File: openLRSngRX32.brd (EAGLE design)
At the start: 40.3 x 36.8 mm, 19 parts, among them IC1 STM32F10XCXT6, IC2 REG1117

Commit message: - remove project - working onwards...
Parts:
- added C1, C10, C11, C2, C3, C4, C5, C6, C7, C8, C9: (no value), SparkFun-Capacitors:0805
- added JP4: (no value), SparkFun-Connectors:1X04
- added JP5, JP6: (no value), SparkFun-Connectors:1X06
- added JP7, JP8: (no value), SparkFun-Connectors:1X02
- added R13, R14, R15, R16: (no value), SparkFun-Resistors:0805
- added U1: MPU-6000QFN-24, SparkFun-Sensors:QFN-24-TESTING
- added Y1: (no value), crystal_3225:CRYSTAL-SMD-5X3
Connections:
- new net BOOT0: IC1.44, JP7.2, R15.2
- new net DTR: JP5.6
- new net MPUINT: U1.12
- new net N$14: C1.2, U1.10
- new net N$15: C2.2, U1.20
- new net N$16: C4.1, IC1.5, Y1.3
- new net N$17: C3.1, IC1.6, Y1.1
- new net N$29: JP5.2
- new net N$35: JP6.3
- new net PPM: IC1.29, JP6.6
- new net RESET: C11.1, IC1.7, JP8.1, R16.1
- new net RX: IC1.31, JP5.4
- new net SCL: IC1.21, JP4.3, R13.1, U1.23
- new net SDA: IC1.22, JP4.2, R14.1, U1.24
- new net TX: IC1.30, JP5.5
- net 3V3: now also C10.1, C5.1, C6.1, C7.1, C8.1, C9.1, JP4.4, JP5.3, JP7.1, R13.2, R14.2, R16.2, U1.13, U1.8
- net GND: now also C1.1, C10.2, C11.2, C2.1, C3.2, C4.2, C5.2, C6.2, C7.2, C8.2, C9.2, JP4.1, JP5.1, JP6.1, JP6.4, JP8.2, R15.1, U1.1, U1.11, U1.18, U1.9, Y1.2, Y1.4
- net VCC: now also JP6.2, JP6.5
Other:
- board size 40.3 x 36.8 mm -> 48.6 x 48.2 mm

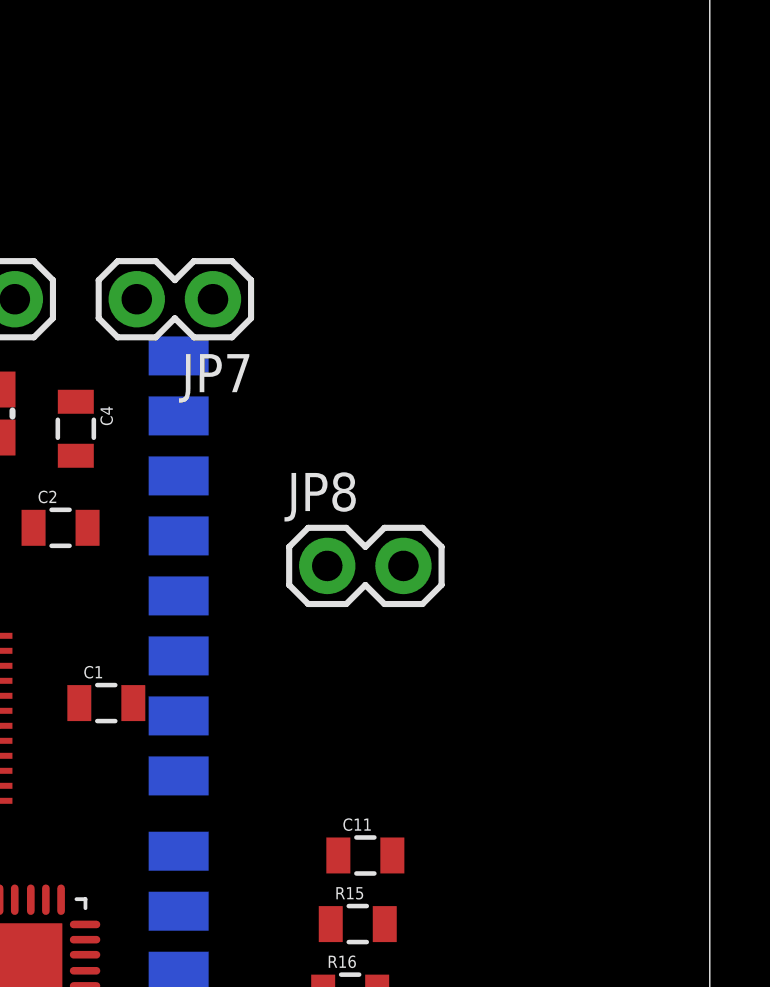
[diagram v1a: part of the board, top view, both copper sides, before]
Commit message: some more caps
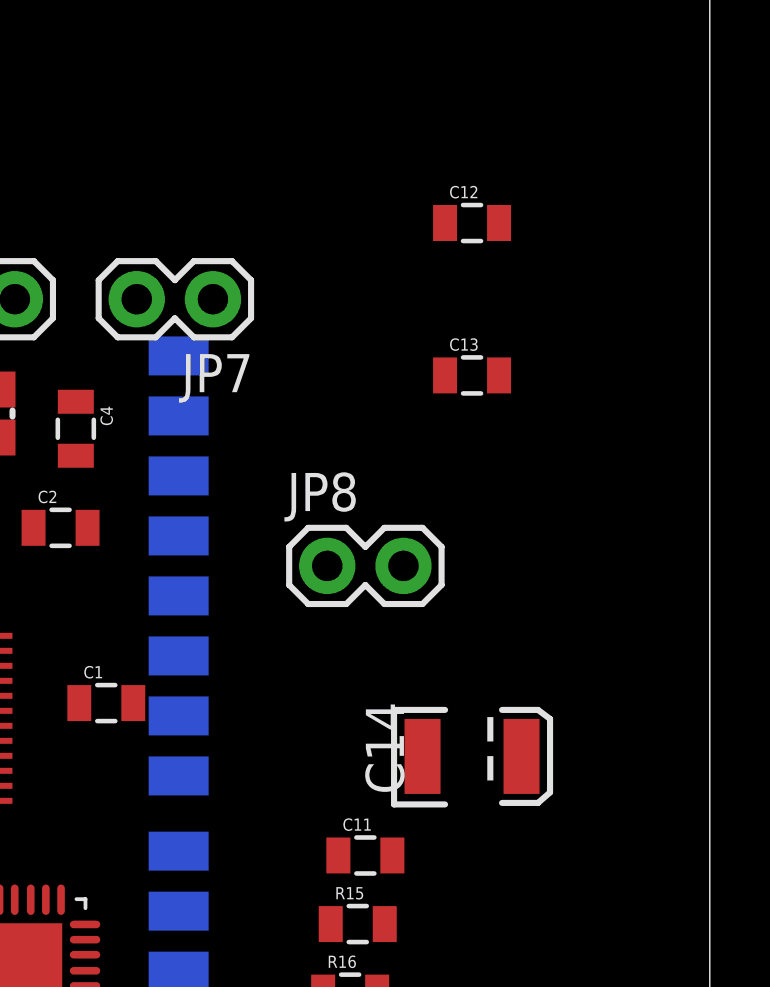
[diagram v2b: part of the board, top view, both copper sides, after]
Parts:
- added C12, C13: (no value), SparkFun-Capacitors:0805
- added C14: 47uF, SparkFun-Capacitors:EIA3528
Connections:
- net 3V3: now also C14.A
- net GND: now also C12.2, C13.2, C14.C
- net VCC: now also C12.1, C13.1
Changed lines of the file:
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@@
 <element name="JP7" library="SparkFun-Connectors" package="1X02" value="" x="32.004" y="35.56" rot="R180"/>
 <element name="JP8" library="SparkFun-Connectors" package="1X02" value="" x="35.814" y="26.67"/>
+<element name="C12" library="SparkFun-Capacitors" package="0805" value="" x="40.64" y="38.1"/>
+<element name="C13" library="SparkFun-Capacitors" package="0805" value="" x="40.64" y="33.02"/>
+<element name="C14" library="SparkFun-Capacitors" package="EIA3528" value="47uF" x="40.64" y="20.32">
+<attribute name="PROD_ID" value="CAP-08310" x="40.64" y="20.32" size="1.778" layer="27" display="off"/>
+</element>
 </elements>
 <signals>
@@
 <contactref element="C11" pad="2"/>
 <contactref element="JP8" pad="2"/>
+<contactref element="C13" pad="2"/>
+<contactref element="C12" pad="2"/>
+<contactref element="C14" pad="C"/>
+<wire x1="30.86" y1="31.67" x2="38.354" y2="26.67" width="0" layer="19" extent="16-16"/>
 <wire x1="27.432" y1="30.342" x2="30.86" y2="31.67" width="0" layer="19" extent="1-16"/>
 <wire x1="26.024" y1="27.94" x2="27.432" y2="30.342" width="0" layer="19" extent="1-1"/>
@@
 <wire x1="2.54" y1="5.08" x2="2.54" y2="7.62" width="0" layer="19" extent="1-1"/>
 <wire x1="2.54" y1="2.54" x2="2.54" y2="5.08" width="0" layer="19" extent="1-1"/>
-<wire x1="38.354" y1="26.67" x2="2.54" y2="2.54" width="0" layer="19" extent="1-1"/>
+<wire x1="41.54" y1="38.1" x2="2.54" y2="2.54" width="0" layer="19" extent="1-1"/>
+<wire x1="41.54" y1="33.02" x2="41.54" y2="38.1" width="0" layer="19" extent="1-1"/>
+<wire x1="38.99" y1="20.32" x2="41.54" y2="33.02" width="0" layer="19" extent="1-1"/>
 </signal>
 <signal name="VCC">
@@
 <contactref element="JP6" pad="5"/>
 <contactref element="JP6" pad="2"/>
+<contactref element="C12" pad="1"/>
+<contactref element="C13" pad="1"/>
+<wire x1="5.08" y1="33.02" x2="12.7" y2="33.02" width="0" layer="19" extent="1-1"/>
+<wire x1="5.08" y1="30.48" x2="5.08" y2="33.02" width="0" layer="19" extent="1-1"/>
 <wire x1="5.08" y1="27.94" x2="5.08" y2="30.48" width="0" layer="19" extent="1-1"/>
 <wire x1="5.08" y1="25.4" x2="5.08" y2="27.94" width="0" layer="19" extent="1-1"/>
@@
 <wire x1="5.08" y1="5.08" x2="5.08" y2="7.62" width="0" layer="19" extent="1-1"/>
 <wire x1="5.08" y1="2.54" x2="5.08" y2="5.08" width="0" layer="19" extent="1-1"/>
-<wire x1="12.7" y1="33.02" x2="5.08" y2="2.54" width="0" layer="19" extent="1-1"/>
-<wire x1="5.08" y1="33.02" x2="12.7" y2="33.02" width="0" layer="19" extent="1-1"/>
+<wire x1="39.74" y1="38.1" x2="5.08" y2="2.54" width="0" layer="19" extent="1-1"/>
+<wire x1="39.74" y1="33.02" x2="39.74" y2="38.1" width="0" layer="19" extent="1-1"/>
 <wire x1="22.1996" y1="8.6614" x2="5.08" y2="7.62" width="0" layer="19" extent="1-1"/>
 </signal>
@@
 <contactref element="R16" pad="2"/>
 <contactref element="JP7" pad="1"/>
-<wire x1="24.82" y1="24.34" x2="25.4" y2="35.56" width="0" layer="19" extent="1-1"/>
+<contactref element="C14" pad="A"/>
+<wire x1="25.4" y1="35.56" x2="32.004" y2="35.56" width="0" layer="19" extent="1-1"/>
+<wire x1="30.86" y1="25.67" x2="32.004" y2="35.56" width="0" layer="19" extent="16-16"/>
+<wire x1="24.82" y1="24.34" x2="30.86" y2="25.67" width="0" layer="19" extent="1-16"/>
 <wire x1="19.07" y1="26.09" x2="24.82" y2="24.34" width="0" layer="19" extent="1-1"/>
-<wire x1="30.86" y1="25.67" x2="24.82" y2="24.34" width="0" layer="19" extent="1-16"/>
 <wire x1="23.07" y1="17.09" x2="24.82" y2="24.34" width="0" layer="19" extent="1-1"/>
 <wire x1="21.728" y1="14.478" x2="23.07" y2="17.09" width="0" layer="19" extent="1-1"/>
@@
 <wire x1="15.82" y1="18.84" x2="21.728" y2="14.478" width="0" layer="19" extent="1-1"/>
 <wire x1="7.62" y1="35.56" x2="19.07" y2="26.09" width="0" layer="19" extent="1-1"/>
-<wire x1="32.004" y1="35.56" x2="22.1996" y2="6.3754" width="0" layer="19" extent="1-1"/>
+<wire x1="42.29" y1="20.32" x2="15.82" y2="18.84" width="0" layer="19" extent="1-1"/>
 </signal>
 <signal name="N$1">

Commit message: board
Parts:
- added J$1, J$2: SMA_EDGE, SparkFun-Connectors:SMA-EDGE
- added JP9: (no value), SparkFun-Connectors:1X03
- added R17: (no value), SparkFun-Resistors:0805
- JP6: device SparkFun-Connectors:1X06 -> SparkFun-Connectors:1X03
- moved JP5 36.1 mm to (16.0, 2.03)
- moved JP4 34.8 mm to (42.4, 10.9), turned to 90 degrees
- moved JP6 31.2 mm to (2.54, 1.78)
- moved IC2 20.8 mm to (39.9, 5.59)
- moved JP8 19.5 mm to (17.0, 32.0), turned to 180 degrees
- moved R14 14.9 mm to (32.8, 23.4)
- moved R13 12.6 mm to (32.0, 19.6)
- moved IC1 10.9 mm to (19.6, 10.7)
- moved U1 6.14 mm to (31.8, 14.2)
- moved U$1 6.04 mm to (28.7, 11.7)
- moved U$2 6.04 mm to (28.7, 28.2)
- moved C6 4.93 mm to (31.8, 8.13)
- moved C5 4.32 mm to (32.0, 2.54)
- moved R4 4.32 mm to (11.4, 18.5)
- moved R5 3.56 mm to (11.4, 16.8)
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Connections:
- removed net N$35: JP6.3
- new net N$13: J$2.SIG, U$2.1
- new net N$18: J$1.SIG, U$1.1
- new net N$19: U$2.4, U$2.6
- new net N$20: U$2.3, U$2.7
- new net N$23: U$1.4, U$1.6
- new net N$24: U$1.3, U$1.7
- new net N$25: JP6.3, R17.1
- net GND: now also J$1.GND@0, J$1.GND@1, J$1.GND@2, J$1.GND@3, J$2.GND@0, J$2.GND@1, J$2.GND@2, J$2.GND@3; no longer JP6.4
- net PPM: now also R17.2; no longer JP6.6
- net VCC: no longer JP6.5
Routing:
- net PWM9: track 20.7 -> 0.00 mm, vias 2 -> 0
- net PWM10: track 16.8 -> 0.00 mm, vias 1 -> 0
- net PWM8: track 10.6 -> 0.00 mm
- net PWM1: track 8.76 -> 16.0 mm
- net PWM2: track 6.82 -> 12.8 mm
- net N$4: track 2.91 -> 7.30 mm
- net PWM7: track 8.69 -> 4.42 mm
- net N$5: track 2.91 -> 6.90 mm
- net PWM3: track 5.53 -> 9.46 mm
- net N$25: track 0.00 -> 3.23 mm
- net N$6: track 2.91 -> 5.78 mm
- net N$7: track 2.91 -> 5.68 mm
- net N$3: track 2.91 -> 5.46 mm
- net PWM4: track 4.10 -> 6.25 mm
- net N$2: track 2.91 -> 4.85 mm
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
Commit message: pcb
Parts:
- added JP10: (no value), SparkFun-Connectors:1X03
- moved JP9 8.52 mm to (14.0, 32.3), turned to 270 degrees
- moved JP8 8.39 mm to (21.8, 25.1)
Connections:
- new net AIN4: IC1.14, JP9.3
- new net AIN5: IC1.15, JP10.3
- net 3V3: now also JP10.2, JP9.2
- net GND: now also JP10.1, JP9.1
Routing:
- net PWM8: track 0.00 -> 3.23 mm
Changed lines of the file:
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@@
 <element name="R16" library="SparkFun-Resistors" package="0805" value="" x="36.576" y="12.446"/>
 <element name="JP7" library="SparkFun-Connectors" package="1X02" value="" x="32.004" y="35.56" rot="R180"/>
-<element name="JP8" library="SparkFun-Connectors" package="1X02" value="" x="17.018" y="32.004" rot="R180"/>
+<element name="JP8" library="SparkFun-Connectors" package="1X02" value="" x="21.844" y="25.146" rot="R180"/>
 <element name="C12" library="SparkFun-Capacitors" package="0805" value="" x="40.64" y="38.1"/>
 <element name="C13" library="SparkFun-Capacitors" package="0805" value="" x="40.64" y="33.02"/>
@@
 <element name="J$2" library="SparkFun-Connectors" package="SMA-EDGE" value="SMA_EDGE" x="45.72" y="25.4" rot="R90"/>
 <element name="JP6" library="SparkFun-Connectors" package="1X03" value="" x="2.54" y="1.778"/>
-<element name="JP9" library="SparkFun-Connectors" package="1X03" value="" x="17.78" y="39.878"/>
 <element name="R17" library="SparkFun-Resistors" package="0805" value="" x="11.43" y="2.54"/>
+<element name="JP9" library="SparkFun-Connectors" package="1X03" value="" x="13.97" y="32.258" rot="R270"/>
+<element name="JP10" library="SparkFun-Connectors" package="1X03" value="" x="16.51" y="32.258" rot="R270"/>
 </elements>
 <signals>
@@
 <contactref element="J$2" pad="GND@3"/>
 <contactref element="JP6" pad="1"/>
+<contactref element="JP10" pad="1"/>
+<contactref element="JP9" pad="1"/>
 <wire x1="41.54" y1="33.02" x2="41.54" y2="38.1" width="0" layer="19" extent="1-1"/>
 <wire x1="36.702" y1="33.194" x2="41.54" y2="33.02" width="0" layer="19" extent="1-16"/>
@@
 <wire x1="20.702" y1="18.684" x2="18.808" y2="15.168" width="0" layer="19" extent="1-16"/>
 <wire x1="20.702" y1="21.194" x2="20.702" y2="18.684" width="0" layer="19" extent="16-16"/>
+<wire x1="19.304" y1="25.146" x2="20.702" y2="21.194" width="0" layer="19" extent="16-16"/>
+<wire x1="23.198" y1="30.188" x2="19.304" y2="25.146" width="0" layer="19" extent="1-1"/>
+<wire x1="24.892" y1="30.342" x2="23.198" y2="30.188" width="0" layer="19" extent="1-1"/>
+<wire x1="26.024" y1="29.718" x2="24.892" y2="30.342" width="0" layer="19" extent="1-1"/>
+<wire x1="20.998" y1="31.788" x2="23.198" y2="30.188" width="0" layer="19" extent="1-1"/>
+<wire x1="19.304" y1="32.142" x2="20.998" y2="31.788" width="0" layer="19" extent="1-1"/>
+<wire x1="16.51" y1="32.258" x2="19.304" y2="32.142" width="0" layer="19" extent="1-1"/>
+<wire x1="13.97" y1="32.258" x2="16.51" y2="32.258" width="0" layer="19" extent="1-1"/>
+<wire x1="20.702" y1="35.194" x2="19.304" y2="32.142" width="0" layer="19" extent="1-16"/>
+<wire x1="27.548" y1="23.876" x2="26.024" y2="29.718" width="0" layer="19" extent="1-1"/>
 <wire x1="21.808" y1="6.168" x2="24.058" y2="12.918" width="0" layer="19" extent="1-1"/>
 <wire x1="20.702" y1="4.684" x2="21.808" y2="6.168" width="0" layer="19" extent="1-16"/>
 <wire x1="16.002" y1="2.032" x2="20.702" y2="4.684" width="0" layer="19" extent="16-16"/>
 <wire x1="15.058" y1="8.418" x2="16.002" y2="2.032" width="0" layer="19" extent="1-1"/>
-<wire x1="27.548" y1="23.876" x2="20.702" y2="21.194" width="0" layer="19" extent="1-16"/>
-<wire x1="26.024" y1="29.718" x2="27.548" y2="23.876" width="0" layer="19" extent="1-1"/>
-<wire x1="24.892" y1="30.342" x2="26.024" y2="29.718" width="0" layer="19" extent="1-1"/>
-<wire x1="23.198" y1="30.188" x2="24.892" y2="30.342" width="0" layer="19" extent="1-1"/>
-<wire x1="20.998" y1="31.788" x2="23.198" y2="30.188" width="0" layer="19" extent="1-1"/>
-<wire x1="19.304" y1="32.142" x2="20.998" y2="31.788" width="0" layer="19" extent="1-1"/>
-<wire x1="20.702" y1="35.194" x2="19.304" y2="32.142" width="0" layer="19" extent="1-16"/>
-<wire x1="14.478" y1="32.004" x2="19.304" y2="32.142" width="0" layer="19" extent="1-1"/>
-<wire x1="2.54" y1="4.318" x2="16.002" y2="2.032" width="0" layer="19" extent="1-1"/>
-<wire x1="2.54" y1="6.858" x2="2.54" y2="4.318" width="0" layer="19" extent="1-1"/>
-<wire x1="2.54" y1="9.398" x2="2.54" y2="6.858" width="0" layer="19" extent="1-1"/>
-<wire x1="2.54" y1="11.938" x2="2.54" y2="9.398" width="0" layer="19" extent="1-1"/>
-<wire x1="2.54" y1="14.478" x2="2.54" y2="11.938" width="0" layer="19" extent="1-1"/>
-<wire x1="2.54" y1="17.018" x2="2.54" y2="14.478" width="0" layer="19" extent="1-1"/>
-<wire x1="2.54" y1="19.558" x2="2.54" y2="17.018" width="0" layer="19" extent="1-1"/>
-<wire x1="2.54" y1="22.098" x2="2.54" y2="19.558" width="0" layer="19" extent="1-1"/>
-<wire x1="2.54" y1="24.638" x2="2.54" y2="22.098" width="0" layer="19" extent="1-1"/>
-<wire x1="2.54" y1="27.178" x2="2.54" y2="24.638" width="0" layer="19" extent="1-1"/>
-<wire x1="2.54" y1="29.718" x2="2.54" y2="27.178" width="0" layer="19" extent="1-1"/>
-<wire x1="2.54" y1="32.258" x2="2.54" y2="29.718" width="0" layer="19" extent="1-1"/>
+<wire x1="2.54" y1="32.258" x2="13.97" y2="32.258" width="0" layer="19" extent="1-1"/>
+<wire x1="2.54" y1="29.718" x2="2.54" y2="32.258" width="0" layer="19" extent="1-1"/>
+<wire x1="2.54" y1="27.178" x2="2.54" y2="29.718" width="0" layer="19" extent="1-1"/>
+<wire x1="2.54" y1="24.638" x2="2.54" y2="27.178" width="0" layer="19" extent="1-1"/>
+<wire x1="2.54" y1="22.098" x2="2.54" y2="24.638" width="0" layer="19" extent="1-1"/>
+<wire x1="2.54" y1="19.558" x2="2.54" y2="22.098" width="0" layer="19" extent="1-1"/>
+<wire x1="2.54" y1="17.018" x2="2.54" y2="19.558" width="0" layer="19" extent="1-1"/>
+<wire x1="2.54" y1="14.478" x2="2.54" y2="17.018" width="0" layer="19" extent="1-1"/>
+<wire x1="2.54" y1="11.938" x2="2.54" y2="14.478" width="0" layer="19" extent="1-1"/>
+<wire x1="2.54" y1="9.398" x2="2.54" y2="11.938" width="0" layer="19" extent="1-1"/>
+<wire x1="2.54" y1="6.858" x2="2.54" y2="9.398" width="0" layer="19" extent="1-1"/>
+<wire x1="2.54" y1="4.318" x2="2.54" y2="6.858" width="0" layer="19" extent="1-1"/>
 <wire x1="2.54" y1="1.778" x2="2.54" y2="4.318" width="0" layer="19" extent="1-1"/>
 </signal>
@@
 <contactref element="JP7" pad="1"/>
 <contactref element="C14" pad="A"/>
+<contactref element="JP9" pad="2"/>
+<contactref element="JP10" pad="2"/>
 <wire x1="36.702" y1="27.194" x2="32.004" y2="35.56" width="0" layer="19" extent="16-16"/>
 <wire x1="33.666" y1="23.368" x2="36.702" y2="27.194" width="0" layer="19" extent="1-16"/>
@@
 <wire x1="22.308" y1="6.168" x2="24.058" y2="13.418" width="0" layer="19" extent="1-1"/>
 <wire x1="21.082" y1="2.032" x2="22.308" y2="6.168" width="0" layer="19" extent="1-1"/>
-<wire x1="15.058" y1="7.918" x2="21.082" y2="2.032" width="0" layer="19" extent="1-1"/>
+<wire x1="15.058" y1="7.918" x2="22.308" y2="6.168" width="0" layer="19" extent="1-1"/>
 <wire x1="43.0276" y1="5.6134" x2="35.676" y2="3.302" width="0" layer="19" extent="1-1"/>
 <wire x1="42.418" y1="18.542" x2="37.476" y2="12.446" width="0" layer="19" extent="1-1"/>
 <wire x1="42.29" y1="20.32" x2="42.418" y2="18.542" width="0" layer="19" extent="1-1"/>
+<wire x1="16.51" y1="29.718" x2="18.308" y2="15.168" width="0" layer="19" extent="1-1"/>
+<wire x1="13.97" y1="29.718" x2="16.51" y2="29.718" width="0" layer="19" extent="1-1"/>
 </signal>
 <signal name="N$1">
@@
 <contactref element="R8" pad="2"/>
 <contactref element="IC1" pad="19"/>
-<wire x1="12.33" y1="11.43" x2="15.058" y2="10.418" width="0" layer="19" extent="1-1"/>
+<wire x1="15.058" y1="10.418" x2="13.204" y2="10.418" width="0.254" layer="1"/>
+<wire x1="13.204" y1="10.418" x2="12.7" y2="10.922" width="0.254" layer="1"/>
+<wire x1="12.7" y1="10.922" x2="12.7" y2="11.06" width="0.254" layer="1"/>
+<wire x1="12.7" y1="11.06" x2="12.33" y2="11.43" width="0.254" layer="1"/>
 </signal>
 <signal name="PWM9">
@@
 <contactref element="JP8" pad="1"/>
 <wire x1="35.676" y1="12.446" x2="36.184" y2="17.018" width="0" layer="19" extent="1-1"/>
-<wire x1="19.308" y1="15.168" x2="35.676" y2="12.446" width="0" layer="19" extent="1-1"/>
-<wire x1="17.018" y1="32.004" x2="19.308" y2="15.168" width="0" layer="19" extent="1-1"/>
+<wire x1="21.844" y1="25.146" x2="36.184" y2="17.018" width="0" layer="19" extent="1-1"/>
+<wire x1="19.308" y1="15.168" x2="21.844" y2="25.146" width="0" layer="19" extent="1-1"/>
 </signal>
 <signal name="BOOT0">
@@
 <wire x1="8.382" y1="2.54" x2="10.53" y2="2.54" width="0.254" layer="1"/>
 </signal>
+<signal name="AIN5">
+<contactref element="IC1" pad="15"/>
+<contactref element="JP10" pad="3"/>
+<wire x1="15.058" y1="12.418" x2="16.51" y2="27.178" width="0" layer="19" extent="1-1"/>
+</signal>
+<signal name="AIN4">
+<contactref element="IC1" pad="14"/>
+<contactref element="JP9" pad="3"/>
+<wire x1="15.058" y1="12.918" x2="13.97" y2="27.178" width="0" layer="19" extent="1-1"/>
+</signal>
 </signals>
